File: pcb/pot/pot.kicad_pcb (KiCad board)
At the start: 2 copper layers, 40.6 x 71.1 mm, 22 parts, among them CON1 Valve, J1 RJ45_LEDS, J2 RJ45, P1 Sensor, Q1 IRLZ44N, Q2 2N3904, Q3 2N3904, U1 PCF8574

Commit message: Add pot PCB
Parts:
- added REF**: MountingHole_2.2mm_M2, Mounting_Holes:MountingHole_2.2mm_M2, F.Cu at (234.9, 81.3)
- added REF**: MountingHole_2.2mm_M2, Mounting_Holes:MountingHole_2.2mm_M2, F.Cu at (234.9, 158.1)
- added REF**: MountingHole_2.2mm_M2, Mounting_Holes:MountingHole_2.2mm_M2, F.Cu at (201.9, 81.3)
- added REF**: MountingHole_2.2mm_M2, Mounting_Holes:MountingHole_2.2mm_M2, F.Cu at (201.9, 158.1)
- J1: value RJ45_LEDS -> Bus
- J2: value RJ45 -> Bus; footprint Connect:RJ45_8 -> Connect:RJHSE538X
- moved F1 129.0 mm to (320.9, 94.9), turned to 180 degrees
- moved D1 121.9 mm to (314.5, 108.3), turned to 180 degrees
- moved Q2 118.5 mm to (320.4, 105.2), turned to 180 degrees
- moved F2 105.9 mm to (302.7, 114.0)
- moved R5 105.0 mm to (309.5, 93.4), turned to 0 degrees
- moved R4 104.3 mm to (302.9, 103.0), turned to 180 degrees
- moved R2 102.4 mm to (302.9, 94.8), turned to 180 degrees
- moved JP4 100.7 mm to (319.2, 111.0), turned to 90 degrees
- moved Q3 97.9 mm to (311.2, 118.1), turned to 180 degrees
- moved U1 87.7 mm to (287.8, 92.1), turned to 270 degrees
- moved JP2 86.6 mm to (241.9, 44.5)
- moved Q1 82.0 mm to (293.6, 115.2), turned to 180 degrees
- moved R3 74.0 mm to (277.4, 105.1)
- moved R6 65.0 mm to (277.4, 113.3), turned to 0 degrees
- moved R1 63.3 mm to (270.7, 112.6), turned to 180 degrees
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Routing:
- net Net-(C1-Pad1): track 112.2 -> 0.00 mm
- net +5V: track 106.0 -> 0.00 mm, vias 1 -> 0
- net Net-(F1-Pad2): track 89.6 -> 0.00 mm, vias 1 -> 0
- net Net-(JP1-Pad1): track 82.6 -> 0.00 mm, vias 1 -> 0
- net Net-(CON1-Pad2): track 80.1 -> 0.00 mm, vias 1 -> 0
- net Net-(J1-Pad6): track 78.2 -> 0.00 mm
- net Net-(J1-Pad8): track 63.3 -> 0.00 mm
- net Net-(JP4-Pad1): track 55.8 -> 0.00 mm, vias 1 -> 0
- net Net-(Q2-Pad1): track 49.5 -> 0.00 mm, vias 1 -> 0
- net +12V: track 42.2 -> 0.00 mm
- net Net-(P1-Pad2): track 37.3 -> 0.00 mm
- net Net-(Q1-Pad2): track 29.6 -> 0.00 mm
- net Net-(Q3-Pad2): track 27.2 -> 0.00 mm
- net Net-(JP4-Pad2): track 26.2 -> 0.00 mm
- net Net-(JP2-Pad2): track 23.9 -> 0.00 mm
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- removed copper zone on B.Cu, net GND
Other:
- board size 40.6 x 71.1 mm -> 38.1 x 81.9 mm

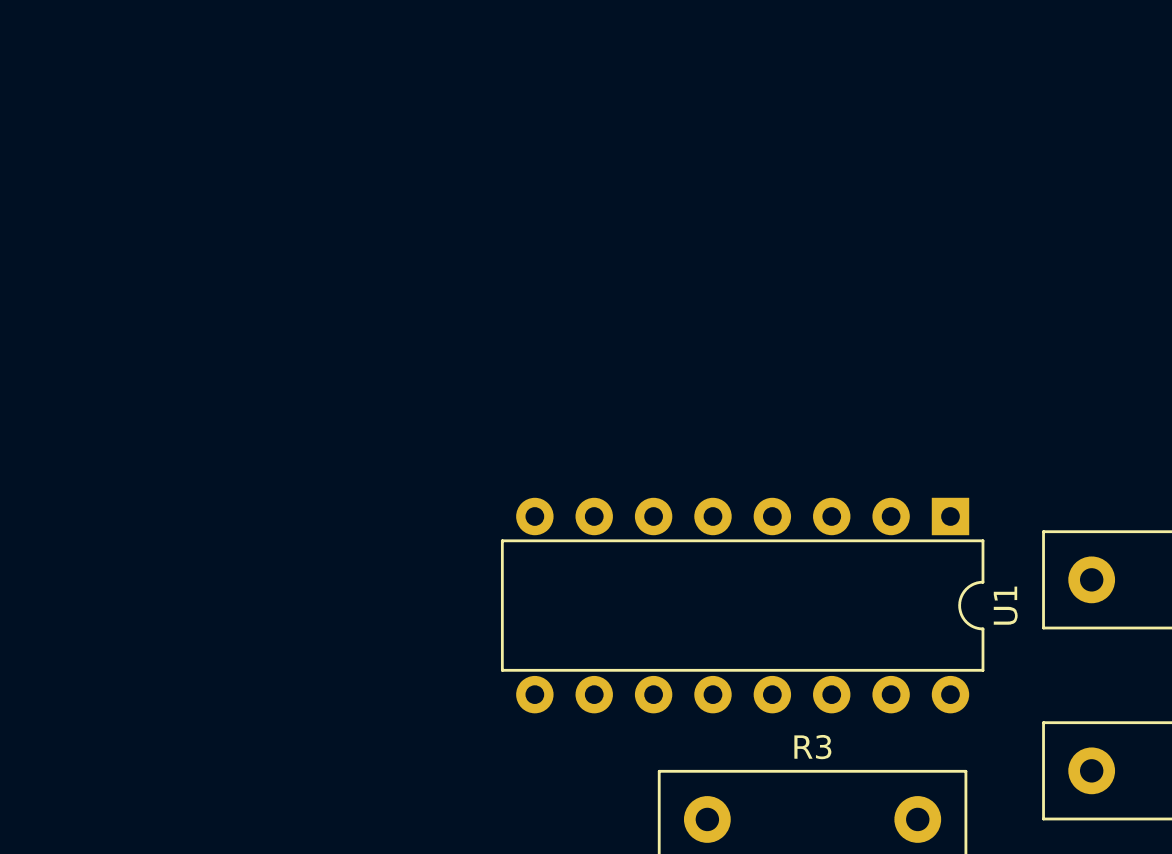
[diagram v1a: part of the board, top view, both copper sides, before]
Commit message: Place pot LED on sensor pin
The sensor pin is most of the times LOW, so it could sink the LED's
current. When reading the sensor the LED will turn off. This will also
help as indicator to see if the pin was successfully restored to LOW
after reading the sensor. Currently the PCF8574 lib doesn't pass any
error codes further. If an LED is off, it's a good indicator for an
invalid state.
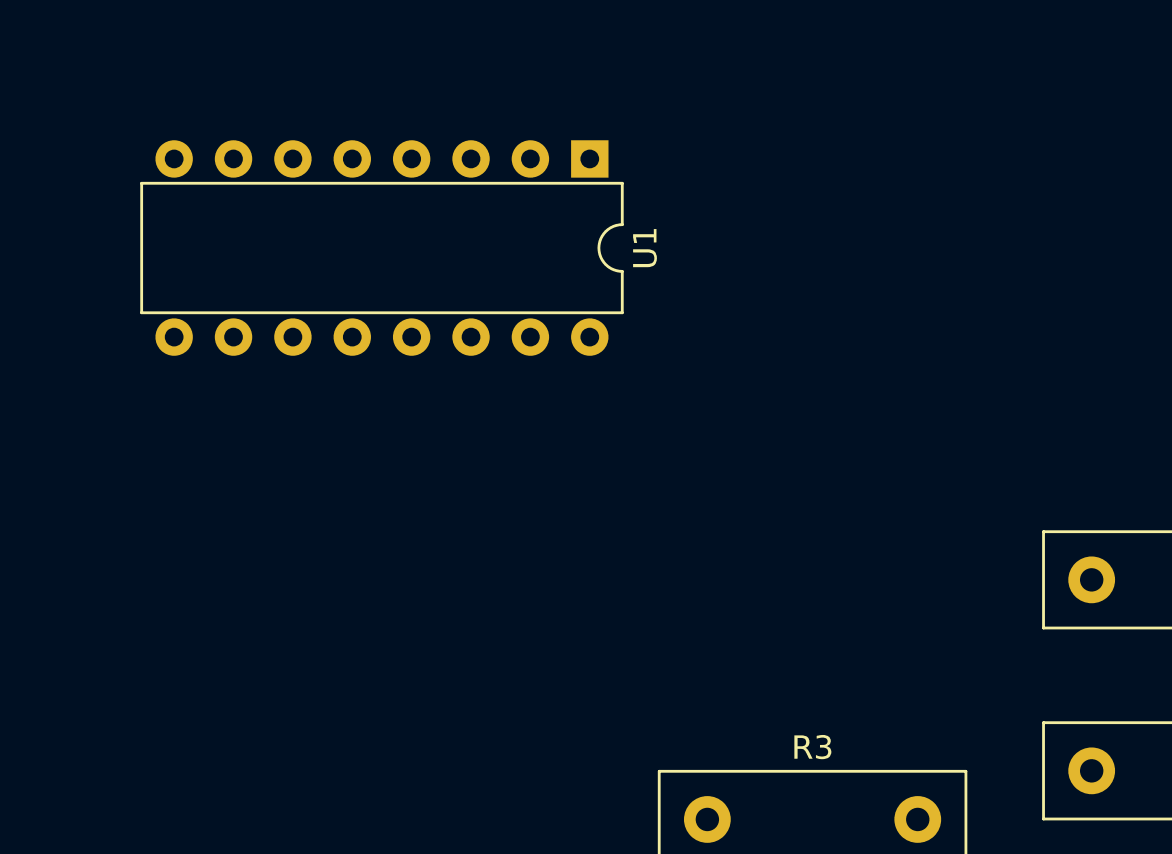
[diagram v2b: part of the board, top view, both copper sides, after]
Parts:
- moved U1 21.7 mm to (272.4, 76.8)
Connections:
- R6 pad 2: Net-(R6-Pad2) -> Net-(JP4-Pad2)
- U1 pad 5: Net-(R6-Pad2) -> Net-(JP4-Pad2)
- U1 pad 6: Net-(JP4-Pad2) -> (no net)
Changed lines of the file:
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@@
     (zones 0)
     (modules 26)
-    (nets 24)
+    (nets 23)
   )
   (page A4)
@@
   (net 20 "Net-(Q3-Pad2)")
   (net 21 "Net-(R4-Pad2)")
-  (net 22 "Net-(R6-Pad2)")
-  (net 23 "Net-(J1-Pad13)")
+  (net 22 "Net-(J1-Pad13)")
   (net_class Default "This is the default net class."
     (clearance 0.2)
@@
     (add_net "Net-(Q3-Pad2)")
     (add_net "Net-(R4-Pad2)")
-    (add_net "Net-(R6-Pad2)")
   )
   (net_class 12V ""
@@
     (fp_line (start 11.87 7.62) (end -4.76 7.62) (layer F.SilkS) (width 0.12))
     (pad 13 thru_hole circle (at 11.68 0.89 270) (size 2 2) (drill 1.57) (layers *.Cu *.Mask)
-      (net 23 "Net-(J1-Pad13)"))
+      (net 22 "Net-(J1-Pad13)"))
     (pad 9 thru_hole circle (at -3.3 6.6 270) (size 1.5 1.5) (drill 0.89) (layers *.Cu *.Mask)
       (net 7 "Net-(J1-Pad9)"))
@@
       (net 20 "Net-(Q3-Pad2)"))
     (pad 2 thru_hole circle (at 9 0) (size 2 2) (drill 1) (layers *.Cu *.Mask)
-      (net 22 "Net-(R6-Pad2)"))
+      (net 15 "Net-(JP4-Pad2)"))
     (model Resistors_THT.3dshapes/R_Box_L13.0mm_W4.0mm_P9.00mm.wrl
       (at (xyz 0 0 0))
@@
   )
   (module Housings_DIP:DIP-16_W7.62mm (layer F.Cu)
-    (at 287.845 92.130001 270)
+    (at 272.415 76.835 270)
     (descr "16-lead dip package, row spacing 7.62 mm (300 mils)")
     (tags "DIL DIP PDIP 2.54mm 7.62mm 300mil")
@@
     (pad 12 thru_hole oval (at 7.62 10.16 270) (size 1.6 1.6) (drill 0.8) (layers *.Cu *.Mask))
     (pad 5 thru_hole oval (at 0 10.16 270) (size 1.6 1.6) (drill 0.8) (layers *.Cu *.Mask)
-      (net 22 "Net-(R6-Pad2)"))
+      (net 15 "Net-(JP4-Pad2)"))
     (pad 13 thru_hole oval (at 7.62 7.62 270) (size 1.6 1.6) (drill 0.8) (layers *.Cu *.Mask))
-    (pad 6 thru_hole oval (at 0 12.7 270) (size 1.6 1.6) (drill 0.8) (layers *.Cu *.Mask)
-      (net 15 "Net-(JP4-Pad2)"))
+    (pad 6 thru_hole oval (at 0 12.7 270) (size 1.6 1.6) (drill 0.8) (layers *.Cu *.Mask))
     (pad 14 thru_hole oval (at 7.62 5.08 270) (size 1.6 1.6) (drill 0.8) (layers *.Cu *.Mask)
       (net 9 "Net-(J1-Pad6)"))
@@
     (pad "" thru_hole circle (at 9.91 -2.54 270) (size 3.3 3.3) (drill 3.3) (layers *.Cu *.Mask))
     (pad 14 thru_hole circle (at -4.57 0.89 270) (size 2 2) (drill 1.57) (layers *.Cu *.Mask)
-      (net 23 "Net-(J1-Pad13)"))
+      (net 22 "Net-(J1-Pad13)"))
     (model Connectors.3dshapes/RJHSE538X.wrl
       (at (xyz 0.14 0.06 0.12))

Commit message: Fix bus switch
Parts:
- R6: value 100k -> 10k
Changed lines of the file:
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@@
       (effects (font (size 1 1) (thickness 0.15)))
     )
-    (fp_text value 100k (at 4.5 3.06) (layer F.Fab)
+    (fp_text value 10k (at 4.5 3.06) (layer F.Fab)
       (effects (font (size 1 1) (thickness 0.15)))
     )
